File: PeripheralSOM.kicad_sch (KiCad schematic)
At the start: 0 parts

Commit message: Initial new commit
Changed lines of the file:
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@@
 	(generator_version "8.0")
 	(paper "A4")
-	(hierarchical_label "+ICAN"
+	(hierarchical_label "GND_PCAN"
 		(shape input)
-		(at 102.87 80.645 0)
+		(at 136.525 82.55 0)
 		(fields_autoplaced yes)
 		(effects
@@
 		)
 	)
-	(hierarchical_label "+12V_ICAN"
+	(hierarchical_label "+PCAN"
 		(shape input)
-		(at 102.87 76.835 0)
+		(at 136.525 88.265 0)
 		(fields_autoplaced yes)
 		(effects
@@
 		)
 	)
-	(hierarchical_label "GND_ICAN"
+	(hierarchical_label "+12V_PCAN"
 		(shape input)
-		(at 102.87 88.265 0)
+		(at 136.525 78.74 0)
 		(fields_autoplaced yes)
 		(effects
@@
 		)
 	)
-	(hierarchical_label "-ICAN"
+	(hierarchical_label "-PCAN"
 		(shape input)
-		(at 102.87 84.455 0)
+		(at 136.525 92.075 0)
 		(fields_autoplaced yes)
 		(effects

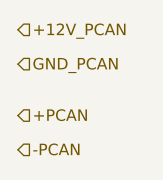
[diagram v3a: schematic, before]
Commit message: Updated Controls + Telemetry
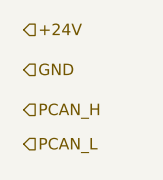
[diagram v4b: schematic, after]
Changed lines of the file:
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@@
 	(generator_version "9.0")
 	(paper "A4")
-	(hierarchical_label "GND_PCAN"
+	(hierarchical_label "GND"
 		(shape input)
-		(at 136.525 82.55 0)
+		(at 137.16 83.185 0)
 		(effects
 			(font
@@
 		)
 	)
-	(hierarchical_label "+PCAN"
+	(hierarchical_label "PCAN_H"
 		(shape input)
-		(at 136.525 88.265 0)
+		(at 137.16 87.63 0)
 		(effects
 			(font
@@
 		)
 	)
-	(hierarchical_label "+12V_PCAN"
+	(hierarchical_label "PCAN_L"
 		(shape input)
-		(at 136.525 78.74 0)
+		(at 137.16 91.44 0)
 		(effects
 			(font
@@
 		)
 	)
-	(hierarchical_label "-PCAN"
+	(hierarchical_label "+24V"
 		(shape input)
-		(at 136.525 92.075 0)
+		(at 137.16 78.74 0)
 		(effects
 			(font
